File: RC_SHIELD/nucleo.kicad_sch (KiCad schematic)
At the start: 1 part

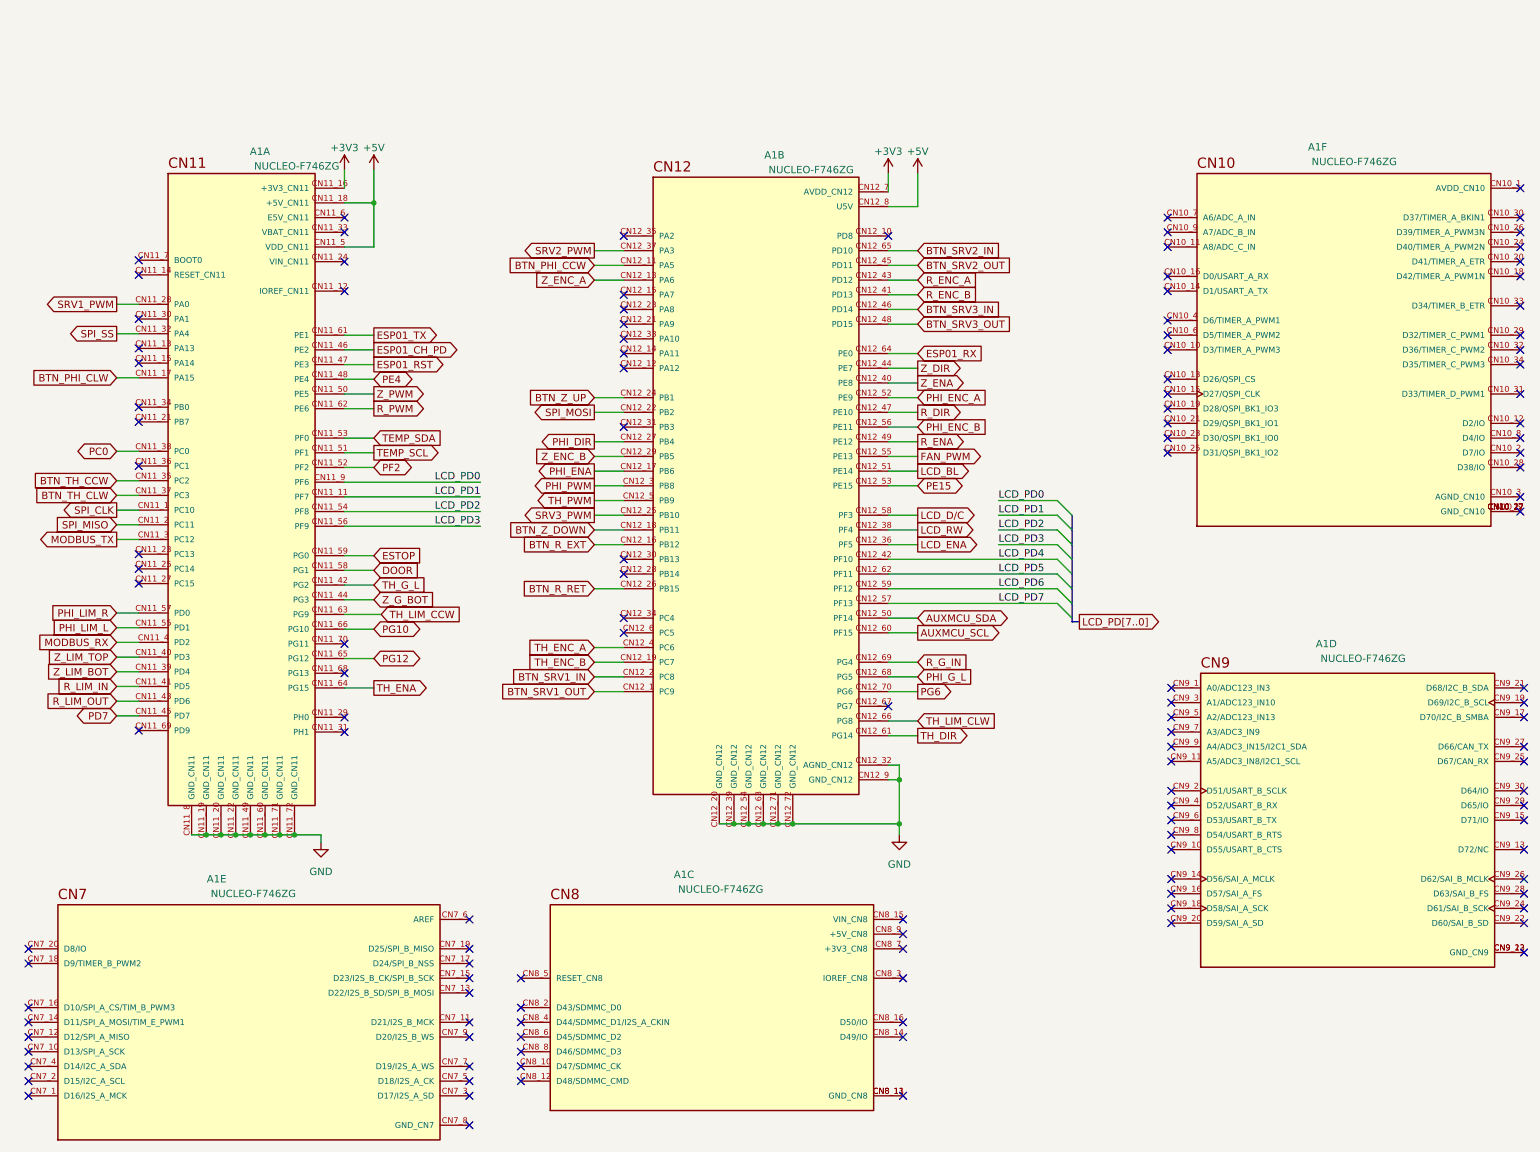
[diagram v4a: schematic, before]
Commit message: Revert "[SCH] reorganized optocouplers and tidied up page 2"
This reverts commit 005640e4067293c5014d1b79d289b32d97da3ff9.
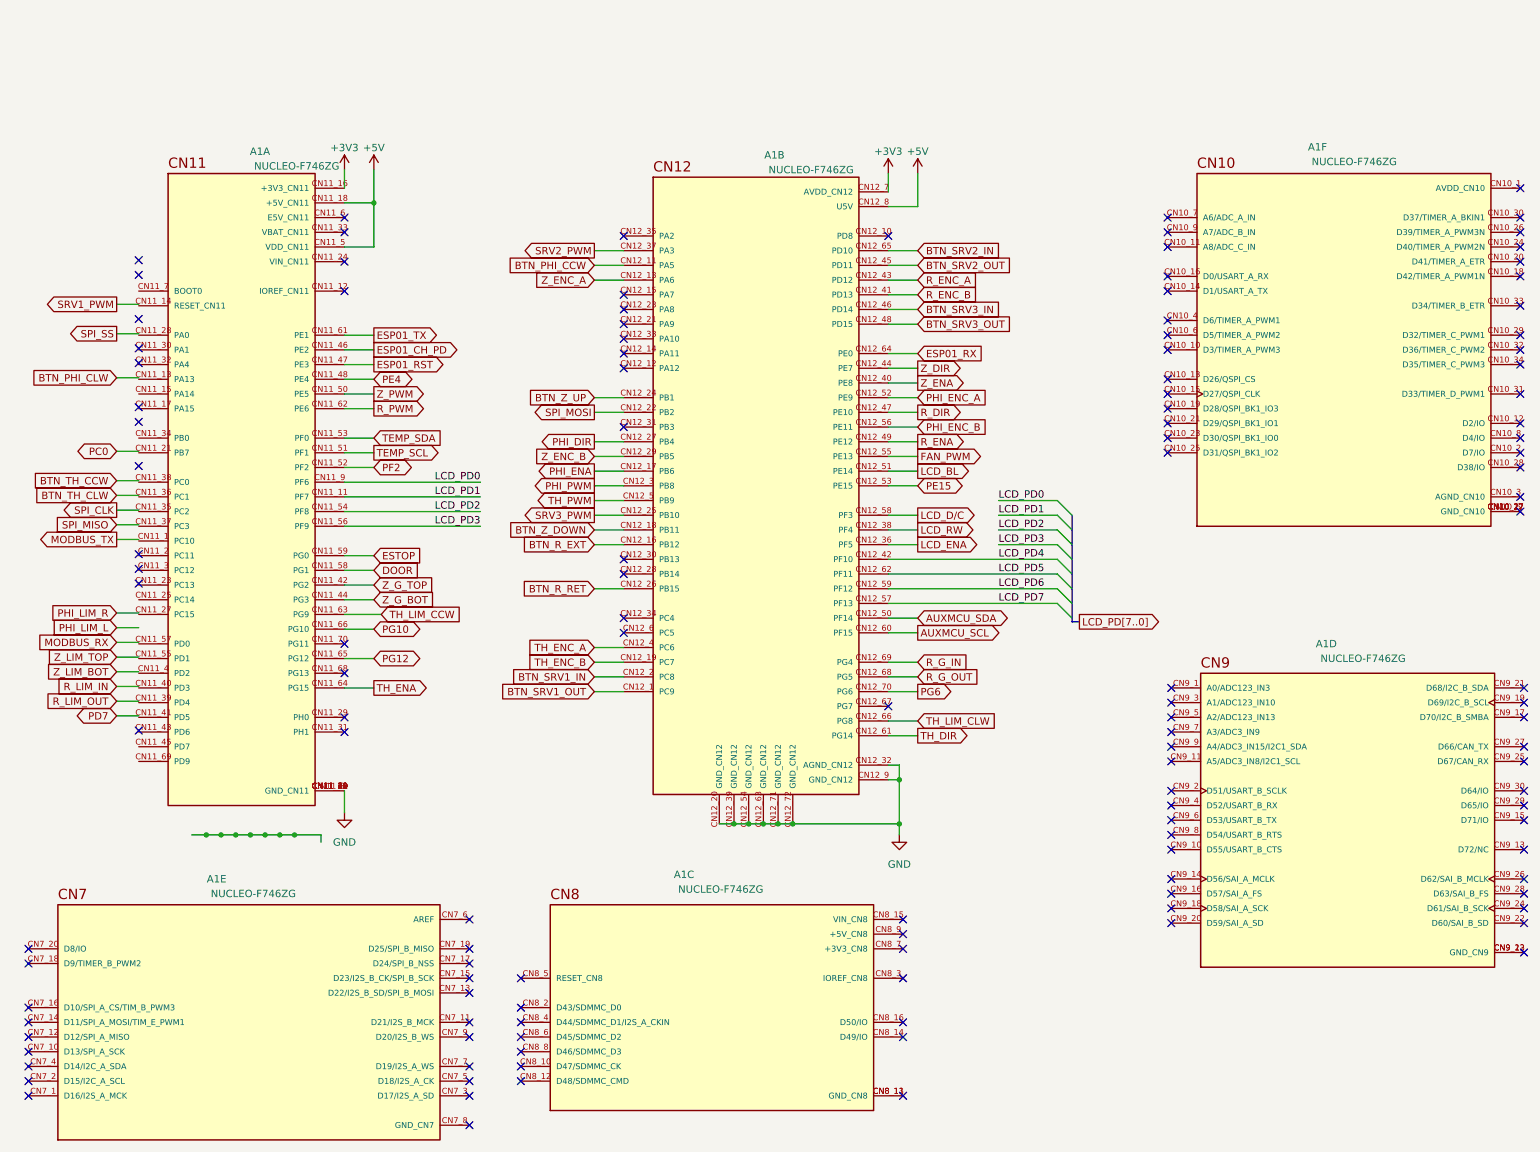
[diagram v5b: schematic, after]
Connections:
- net BTN_PHI_CLW: no longer A1.CN11_17 (PA15)
- net BTN_TH_CCW: no longer A1.CN11_35 (PC2)
- net BTN_TH_CLW: no longer A1.CN11_37 (PC3)
- net MODBUS_RX: no longer A1.CN11_4 (PD2)
- net MODBUS_TX: no longer A1.CN11_3 (PC12)
- net PC0: no longer A1.CN11_38 (PC0)
- net PD7: no longer A1.CN11_45 (PD7)
- net PHI_LIM_L: no longer A1.CN11_55 (PD1)
- net PHI_LIM_R: no longer A1.CN11_57 (PD0)
- net R_LIM_IN: no longer A1.CN11_41 (PD5)
- net R_LIM_OUT: no longer A1.CN11_43 (PD6)
- net SPI_CLK: no longer A1.CN11_1 (PC10)
- net SPI_MISO: no longer A1.CN11_2 (PC11)
- net SPI_SS: no longer A1.CN11_32 (PA4)
- net SRV1_PWM: no longer A1.CN11_28 (PA0)
- net Z_LIM_BOT: no longer A1.CN11_39 (PD4)
- net Z_LIM_TOP: no longer A1.CN11_40 (PD3)
- net PHI_G_L renamed R_G_OUT
- net TH_G_L renamed Z_G_TOP
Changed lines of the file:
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@@
+    (stroke (width 0) (type default))
+  )
+  (wire (pts (xy 73.66 129.54) (xy 73.66 133.35))
     (stroke (width 0) (type default))
   )
@@
     )
   )
-  (global_label "PHI_G_L" (shape input) (at 172.72 109.855 0)
+  (global_label "R_G_OUT" (shape input) (at 172.72 109.855 0)
     (effects (font (size 1.27 1.27)) (justify left))
     (property "Intersheetrefs" "${INTERSHEET_REFS}" (at 182.88 109.855 0)
@@
     )
   )
-  (global_label "TH_G_L" (shape input) (at 78.74 93.98 0)
+  (global_label "Z_G_TOP" (shape input) (at 78.74 93.98 0)
     (effects (font (size 1.27 1.27)) (justify left))
     (property "Intersheetrefs" "${INTERSHEET_REFS}" (at 88.779 93.98 0)
@@
     )
   )
-  (symbol (lib_id "power:GND") (at 69.596 138.43 0) (unit 1)
+  (symbol (lib_id "power:GND") (at 73.66 133.35 0) (unit 1)
     (in_bom yes) (on_board yes) (dnp no) (fields_autoplaced)
-    (property "Reference" "#PWR02" (at 69.596 144.78 0)
+    (property "Reference" "#PWR02" (at 73.66 139.7 0)
       (effects (font (size 1.27 1.27)) hide)
     )
-    (property "Value" "GND" (at 69.596 143.51 0)
+    (property "Value" "GND" (at 73.66 138.43 0)
       (effects (font (size 1.27 1.27)))
     )
-    (property "Footprint" "" (at 69.596 138.43 0)
+    (property "Footprint" "" (at 73.66 133.35 0)
       (effects (font (size 1.27 1.27)) hide)
     )
-    (property "Datasheet" "" (at 69.596 138.43 0)
+    (property "Datasheet" "" (at 73.66 133.35 0)
       (effects (font (size 1.27 1.27)) hide)
     )

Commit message: [SCH] fixed Nucleo papercuts
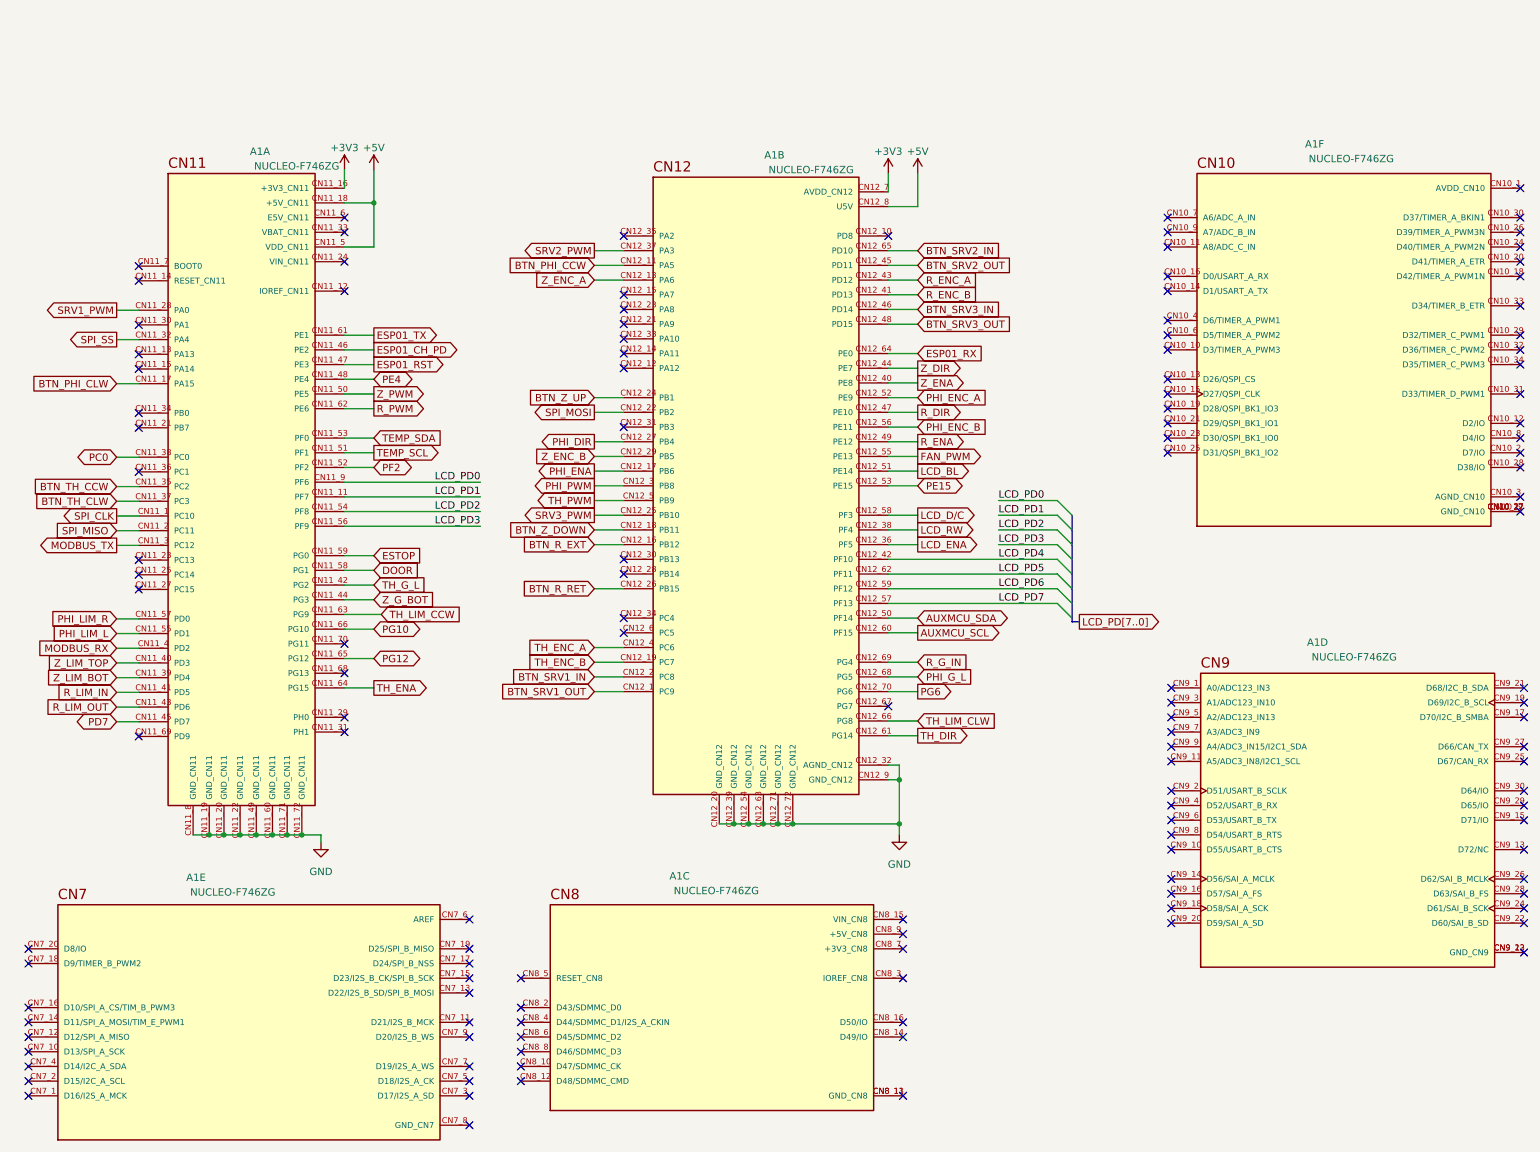
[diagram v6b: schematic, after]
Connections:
- net BTN_PHI_CLW: now also A1.CN11_17 (PA15)
- net BTN_TH_CCW: now also A1.CN11_35 (PC2)
- net BTN_TH_CLW: now also A1.CN11_37 (PC3)
- net MODBUS_RX: now also A1.CN11_4 (PD2)
- net MODBUS_TX: now also A1.CN11_3 (PC12)
- net PC0: now also A1.CN11_38 (PC0)
- net PD7: now also A1.CN11_45 (PD7)
- net PHI_LIM_L: now also A1.CN11_55 (PD1)
- net PHI_LIM_R: now also A1.CN11_57 (PD0)
- net R_LIM_IN: now also A1.CN11_41 (PD5)
- net R_LIM_OUT: now also A1.CN11_43 (PD6)
- net SPI_CLK: now also A1.CN11_1 (PC10)
- net SPI_MISO: now also A1.CN11_2 (PC11)
- net SPI_SS: now also A1.CN11_32 (PA4)
- net SRV1_PWM: now also A1.CN11_28 (PA0)
- net Z_LIM_BOT: now also A1.CN11_39 (PD4)
- net Z_LIM_TOP: now also A1.CN11_40 (PD3)
- net R_G_OUT renamed PHI_G_L
- net Z_G_TOP renamed TH_G_L
